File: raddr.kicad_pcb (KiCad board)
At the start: 2 copper layers, 17.2 x 17 mm, 6 parts, among them J1 Conn_01x07, J3 Conn_01x07, U1 PMS150C-U06

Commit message: Muck around about traces
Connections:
- LED1 pad 2: Net-(J1-Pin_7) -> Net-(J3-Pin_7)
- LED1 pad 3: Net-(J3-Pin_7) -> Net-(J1-Pin_7)
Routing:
- net Net-(J1-Pin_7): track 15.4 -> 7.53 mm
- net Net-(J3-Pin_7): track 12.4 -> 5.33 mm
- net Net-(J3-Pin_6): track 19.7 -> 14.9 mm
- net GND: track 31.0 -> 35.5 mm, vias 0 -> 2
- net +5VD: track 25.9 -> 23.5 mm, vias 2 -> 3
- net Net-(U1-PA3): track 16.9 -> 16.5 mm, vias 2 -> 0

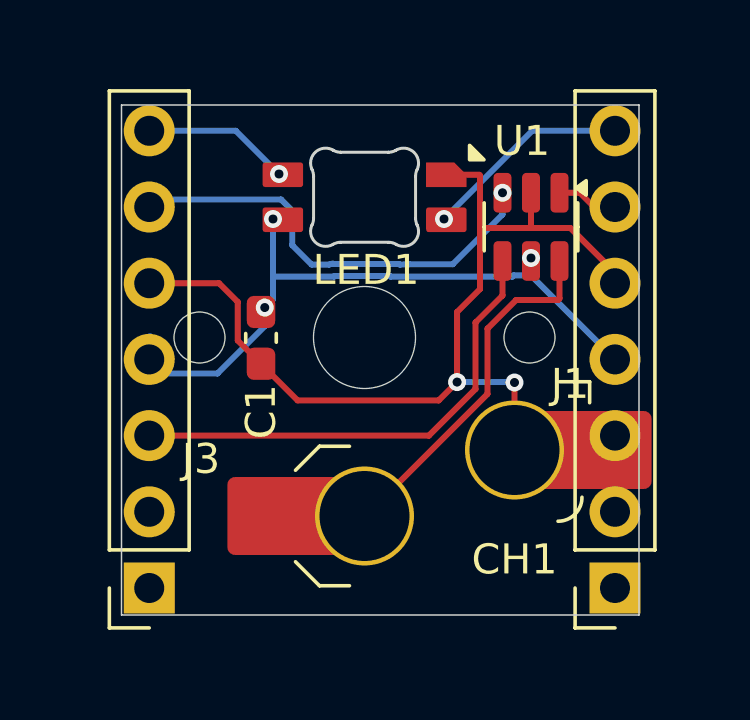
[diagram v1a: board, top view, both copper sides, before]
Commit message: WFP correction factor
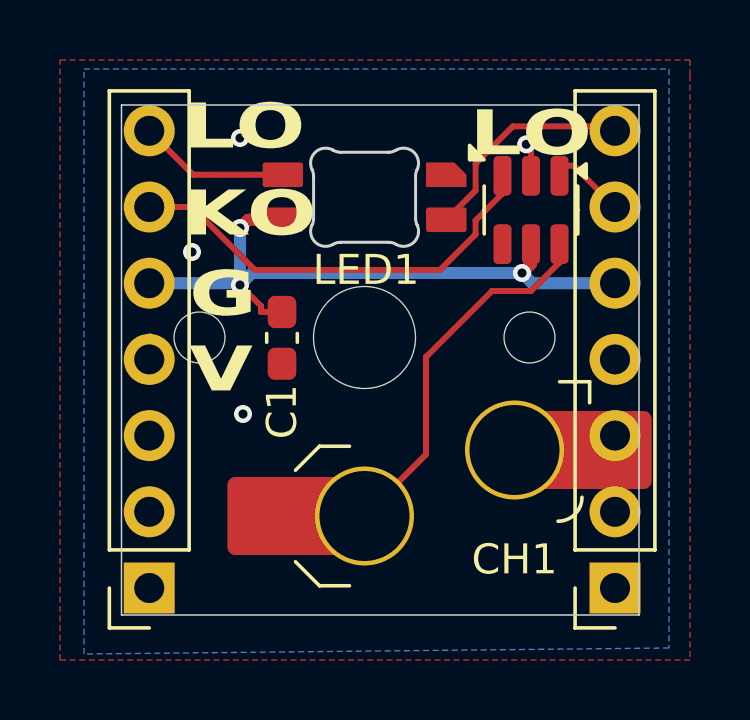
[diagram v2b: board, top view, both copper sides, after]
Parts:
- moved C1 0.70 mm to (147.4, 101.8)
- moved U1 0.56 mm to (155.7, 97.5)
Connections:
- net Net-(J1-Pin_6) renamed KEY_DIN
- net Net-(J1-Pin_7) renamed LED_DIN
- net Net-(J3-Pin_6) renamed KEY_DOUT
- net Net-(J3-Pin_7) renamed LED_DOUT
- net Net-(U1-PA3) renamed SWITCH
- J1 pad 3: unconnected-(J1-Pin_3-Pad3) -> GND
- J1 pad 4: +5VD -> GND
- J1 pad 5: GND -> +5VD
- J3 pad 3: Net-(J3-Pin_3) -> GND
- J3 pad 4: +5VD -> GND
- J3 pad 5: GND -> +5VD
- U1 pad 4: Net-(J3-Pin_3) -> unconnected-(U1-PA5-Pad4)
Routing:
- net GND: track 35.5 -> 3.65 mm, vias 2 -> 4
- net Net-(J3-Pin_3): track 15.6 -> 0.00 mm
- net KEY_DIN: track 2.05 -> 3.12 mm
- net LED_DIN: track 7.53 -> 8.11 mm, vias 1 -> 0
- net LED_DOUT: track 5.33 -> 5.47 mm, vias 1 -> 0
- net KEY_DOUT: vias 1 -> 0
- added copper zone on B.Cu, net GND
- added copper zone on F.Cu, net GND
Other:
- board text added: "G"
- board text added: "KO"
- board text added: "LO"
- board text added: "V"

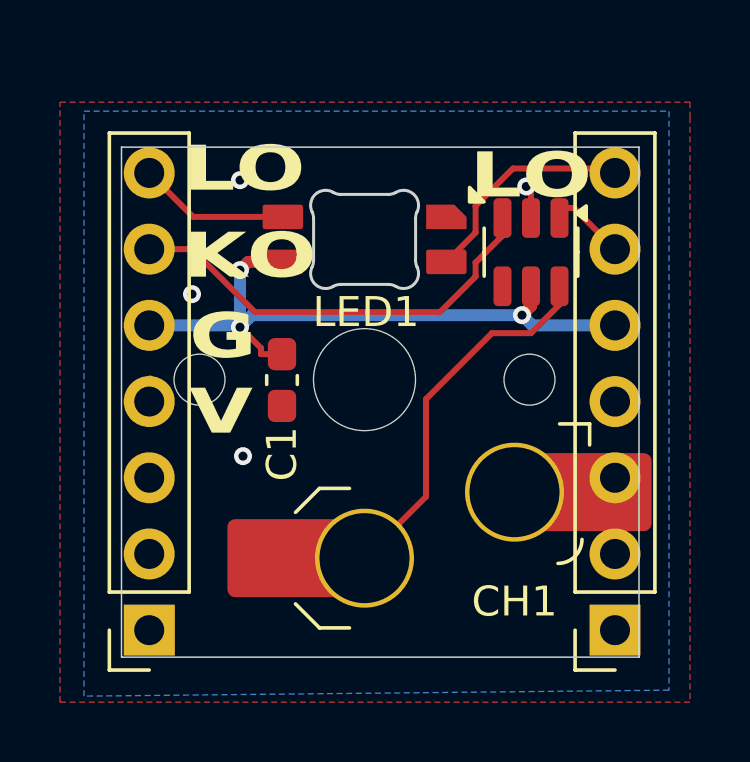
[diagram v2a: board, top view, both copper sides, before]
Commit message: split connector
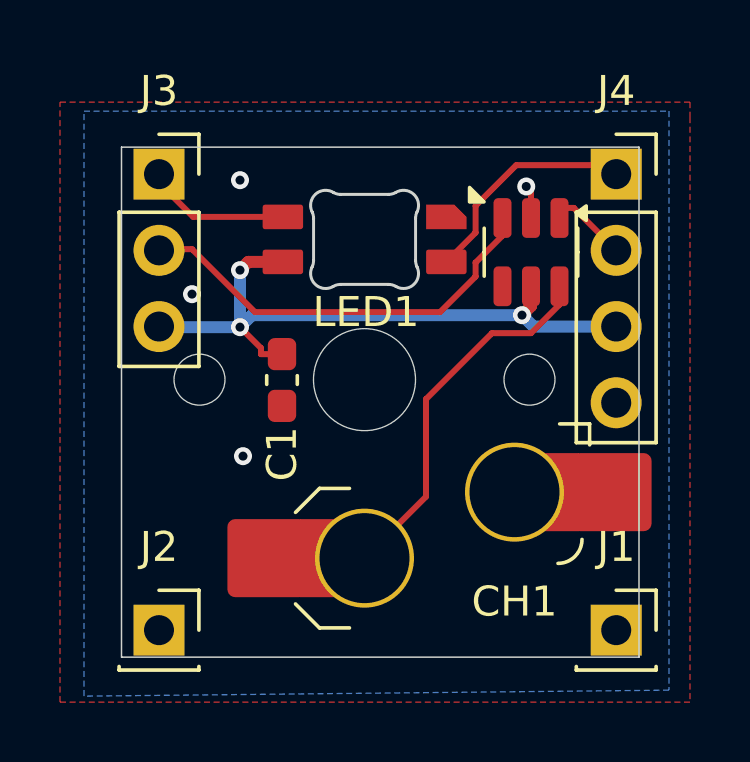
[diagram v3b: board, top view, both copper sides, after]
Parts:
- added J2: Conn_01x01, Connector_PinSocket_2.54mm:PinSocket_1x01_P2.54mm_Vertical, F.Cu at (143.3, 110.1)
- added J4: Conn_01x04, Connector_PinSocket_2.54mm:PinSocket_1x04_P2.54mm_Vertical, F.Cu at (158.5, 94.9)
- J1: value Conn_01x07 -> Conn_01x01; footprint Connector_PinSocket_2.54mm:PinSocket_1x07_P2.54mm_Vertical -> Connector_PinSocket_2.54mm:PinSocket_1x01_P2.54mm_Vertical
- J3: value Conn_01x07 -> Conn_01x03; footprint Connector_PinSocket_2.54mm:PinSocket_1x07_P2.54mm_Vertical -> Connector_PinSocket_2.54mm:PinSocket_1x03_P2.54mm_Vertical
- moved J3 15.2 mm to (143.3, 94.9), turned to 0 degrees
- turned J1 to 0 degrees
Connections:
- J1 pad 1: unconnected-(J1-Pin_1-Pad1) -> GND
- J3 pad 1: unconnected-(J3-Pin_1-Pad1) -> LED_DOUT
- J3 pad 2: unconnected-(J3-Pin_2-Pad2) -> KEY_DOUT
- J3 pad 3: GND -> +5VD
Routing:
- net +5VD: track 23.5 -> 22.4 mm
- net GND: track 3.65 -> 2.91 mm
- net KEY_DIN: track 3.12 -> 2.48 mm

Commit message: silk screen
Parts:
- moved C1 2.92 mm to (144.9, 100.2)
- moved J3 2.92 mm to (140.8, 93.3)
- moved LED1 2.92 mm to (147.7, 95.5)
- moved CH1 2.92 mm to (147.7, 100.2)
- moved J2 2.92 mm to (140.8, 108.5)
- moved J4 2.92 mm to (156.1, 93.3)
- moved J1 2.92 mm to (156.1, 108.5)
- moved U1 2.92 mm to (153.2, 95.9)
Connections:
- J3 pad 3: +5VD -> PROG_VPP
- U1 pad 4: unconnected-(U1-PA5-Pad4) -> PROG_VPP
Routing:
- net PROG_VPP: track 0.00 -> 12.1 mm
- net +5VD: track 22.4 -> 17.7 mm
- net GND: track 2.91 -> 2.09 mm, vias 4 -> 1
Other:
- board size 17.2 x 17 mm -> 20.8 x 20.6 mm
- board text added: "KI"
- board text added: "LI"
- board text added: "VCC"
- board text removed: "V"

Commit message: Silk screen adjustments.
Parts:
- renumbered J3 to J1, J4 to J3, J1 to J4
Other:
- board size 20.8 x 20.6 mm -> 15.3 x 17.9 mm
- board text added: "VPP"
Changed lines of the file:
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@@
 		(descr "Through hole straight socket strip, 1x01, 2.54mm pitch, single row (from Kicad 4.0.7), script generated")
 		(tags "Through hole socket strip THT 1x01 2.54mm single row")
-		(property "Reference" "J1"
+		(property "Reference" "J4"
 			(at 0 -2.77 0)
 			(layer "F.SilkS")
@@
 		(descr "Through hole straight socket strip, 1x04, 2.54mm pitch, single row (from Kicad 4.0.7), script generated")
 		(tags "Through hole socket strip THT 1x04 2.54mm single row")
-		(property "Reference" "J4"
+		(property "Reference" "J3"
 			(at 0 -2.77 0)
 			(layer "F.SilkS")
@@
 			(size 1.7 1.7)
 			(drill 1)
+			(property pad_prop_castellated)
 			(layers "*.Cu" "*.Mask")
 			(remove_unused_layers no)
@@
 			(size 1.7 1.7)
 			(drill 1)
+			(property pad_prop_castellated)
 			(layers "*.Cu" "*.Mask")
 			(remove_unused_layers no)
@@
 			(size 1.7 1.7)
 			(drill 1)
+			(property pad_prop_castellated)
 			(layers "*.Cu" "*.Mask")
 			(remove_unused_layers no)
@@
 		(fp_arc
 			(start 1.699999 -0.702841)
-			(mid 1.712533 -0.814065)
+			(mid 1.712531 -0.814066)
 			(end 1.749484 -0.919719)
 			(stroke
@@
 			(at 0 -2.77 0)
 			(layer "F.SilkS")
+			(hide yes)
 			(effects
 				(font
@@
 			(at 0 2.77 0)
 			(layer "F.Fab")
+			(hide yes)
 			(effects
 				(font
@@
 		(descr "Through hole straight socket strip, 1x03, 2.54mm pitch, single row (from Kicad 4.0.7), script generated")
 		(tags "Through hole socket strip THT 1x03 2.54mm single row")
-		(property "Reference" "J3"
+		(property "Reference" "J1"
 			(at 0 -2.77 0)
 			(layer "F.SilkS")
+			(hide yes)
 			(effects
 				(font
@@
 			(at 0 7.85 0)
 			(layer "F.Fab")
+			(hide yes)
 			(effects
 				(font
@@
 	)
 	(gr_rect
-		(start 137.748 90.632)
-		(end 158.576 111.208)
+		(start 140.8468 91.9528)
+		(end 156.1376 109.8872)
 		(stroke
 			(width 0.05)
@@
 		(layer "Edge.Cuts")
 	)
-	(gr_text "KO"
-		(at 146.05 97.155 0)
+	(gr_text "G"
+		(at 155.2448 108.5596 0)
 		(layer "B.SilkS" knockout)
 		(effects
 			(font
-				(size 1.5 2)
-				(thickness 0.375)
+				(size 1.1 2)
+				(thickness 0.275)
 				(bold yes)
 			)
-			(justify left bottom mirror)
+			(justify left mirror)
 		)
 	)
-	(gr_text "G"
-		(at 155.448 102.362 0)
+	(gr_text "LO"
+		(at 145.6944 93.4212 0)
 		(layer "B.SilkS" knockout)
 		(effects
 			(font
-				(size 1 2)
-				(thickness 0.25)
+				(size 1.1 2)
+				(thickness 0.275)
 				(bold yes)
 			)
-			(justify left bottom mirror)
+			(justify left mirror)
 		)
 	)
-	(gr_text "VCC"
-		(at 155.194 99.06 0)
+	(gr_text "G"
+		(at 143.9926 108.6104 0)
 		(layer "B.SilkS" knockout)
 		(effects
 			(font
-				(size 1 2)
-				(thickness 0.25)
+				(size 1.1 2)
+				(thickness 0.275)
 				(bold yes)
 			)
-			(justify left bottom mirror)
+			(justify left mirror)
 		)
 	)
-	(gr_text "LI"
-		(at 155.448 94.488 0)
+	(gr_text "KO"
+		(at 146.05 95.8342 0)
 		(layer "B.SilkS" knockout)
 		(effects
 			(font
-				(size 1.5 2)
-				(thickness 0.375)
+				(size 1.1 2)
+				(thickness 0.275)
 				(bold yes)
 			)
-			(justify left bottom mirror)
+			(justify left mirror)
 		)
 	)
-	(gr_text "KI\n"
-		(at 155.448 97.028 0)
+	(gr_text "LI"
+		(at 155.3258 93.3808 0)
 		(layer "B.SilkS" knockout)
 		(effects
 			(font
-				(size 1.5 2)
-				(thickness 0.375)
+				(size 1.1 2)
+				(thickness 0.275)
 				(bold yes)
 			)
-			(justify left bottom mirror)
+			(justify left mirror)
 		)
 	)
-	(gr_text "LO"
-		(at 145.796 94.615 -0)
+	(gr_text "VCC"
+		(at 155.0464 98.425 0)
 		(layer "B.SilkS" knockout)
 		(effects
 			(font
-				(size 1.5 2)
-				(thickness 0.375)
+				(size 1.1 2)
+				(thickness 0.275)
 				(bold yes)
 			)
-			(justify left bottom mirror)
+			(justify left mirror)
 		)
 	)
+	(gr_text "VPP"
+		(at 147.5994 98.5012 0)
+		(layer "B.SilkS" knockout)
+		(effects
+			(font
+				(size 1.1 2)
+				(thickness 0.275)
+				(bold yes)
+			)
+			(justify left mirror)
+		)
+	)
+	(gr_text "G"
+		(at 156.2402 102.7938 0)
+		(layer "B.SilkS" knockout)
+		(effects
+			(font
+				(size 1.1 2)
+				(thickness 0.275)
+				(bold yes)
+			)
+			(justify left mirror)
+		)
+	)
+	(gr_text "KI"
+		(at 155.3276 95.9046 0)
+		(layer "B.SilkS" knockout)
+		(effects
+			(font
+				(size 1.1 2)
+				(thickness 0.275)
+				(bold yes)
+			)
+			(justify left mirror)
+		)
+	)

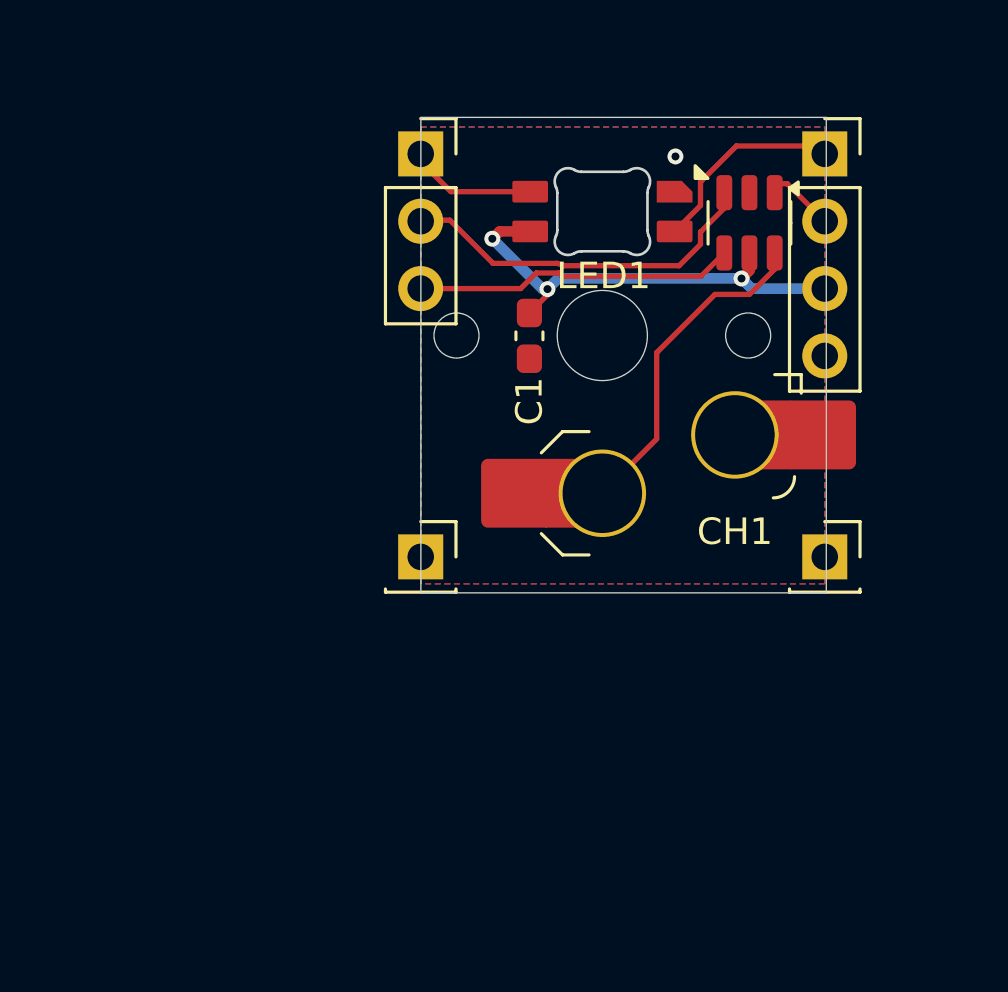
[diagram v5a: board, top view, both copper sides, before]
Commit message: overhaul
- Align on grid
- fillet
- shring X dim
- center button
- remove extra bttn holes
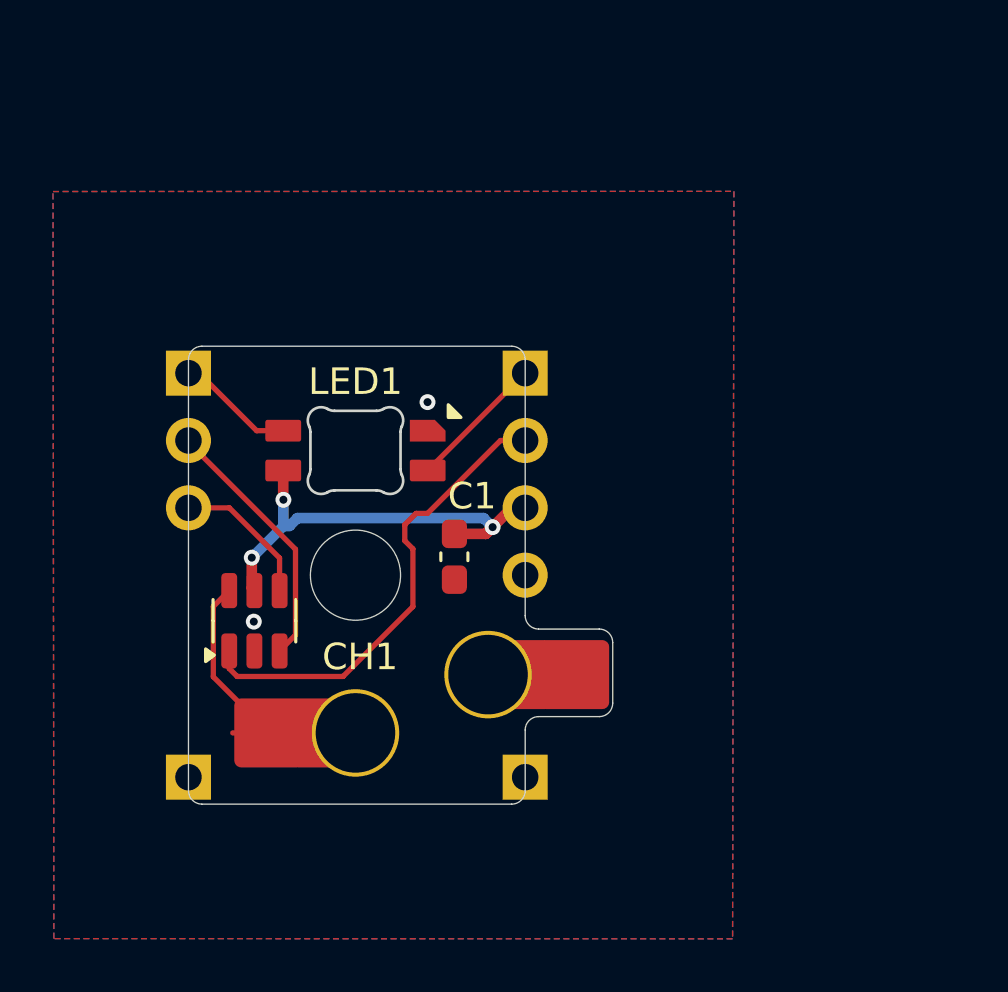
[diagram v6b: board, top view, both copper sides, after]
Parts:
- moved U1 24.0 mm to (134.6, 110.9), turned to 90 degrees
- moved J4 14.0 mm to (144.8, 116.8)
- moved J3 14.0 mm to (144.8, 101.6)
- moved CH1 13.0 mm to (138.4, 109.2)
- moved LED1 13.0 mm to (138.4, 104.5)
- moved J2 12.1 mm to (132.1, 116.8)
- moved J1 12.0 mm to (132.1, 101.6)
- moved C1 8.80 mm to (142.1, 108.5)
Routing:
- net KEY_DIN: track 2.48 -> 17.5 mm
- net SWITCH: track 16.9 -> 7.88 mm
- net PROG_VPP: track 12.1 -> 5.05 mm
- net KEY_DOUT: track 14.6 -> 9.69 mm
- net LED_DIN: track 7.73 -> 5.03 mm
- net GND: track 2.09 -> 0.40 mm, vias 1 -> 2
- net +5VD: track 17.7 -> 16.2 mm
- net LED_DOUT: track 5.47 -> 4.07 mm
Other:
- board size 15.3 x 17.9 mm -> 16 x 17.3 mm
- board text removed: "G"
- board text removed: "KI"
- board text removed: "KO"
- board text removed: "LI"
- board text removed: "LO"
- board text removed: "VCC"
- board text removed: "VPP"
